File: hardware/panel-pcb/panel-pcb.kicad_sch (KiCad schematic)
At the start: 143 parts, among them J1 USB_C_Receptacle_USB2.0_16P, J10 RS-485 OUT, J11 12V_OUT, J2 SWD, J3 FSR North, J4 FSR East, J5 12V_IN, J6 FSR South, J7 FSR West, J8 RS-485 IN, J9 INT OUT, SW1 PANEL_ID, SW2 BOOTSEL, SW3 RS-485 Termination, U1 RP2040, U2 THVD1429, U3 W25Q32JV, U4 SN74AHCT125, U5 AMS1117-5.0, U6 AP7361C-33ER-13, U7 USBLC6-2SC6, U8 LM66200, X1 12MHz ABM8-272-T3

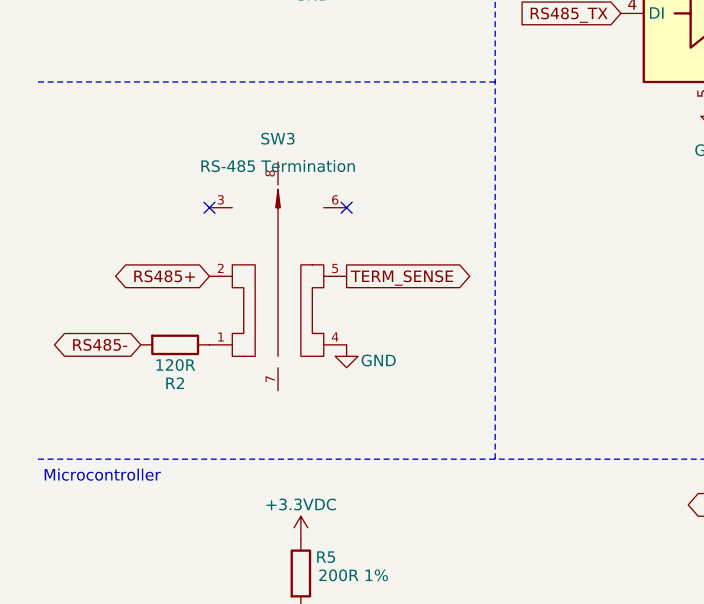
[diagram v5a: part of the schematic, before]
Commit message: Both boards: J9/J4 to the vendor WJ500V land pattern; WS2815 cap question closed
Terminal blocks now use the footprint published by the manufacturer of the part
we actually buy (KANGNEX WJ500V-5.08-2P, LCSC C8465), pulled via easyeda2kicad,
replacing the hand-built Adam Tech MRR52 pattern:
- new panel-pcb/master-pcb:TerminalBlock_WJ500V-5.08-2P (hole 1.30mm per the
  vendor recommendation vs our 1.50mm, pad 2.00mm, origin centred between pins)
  plus the vendor 3D model, which supersedes the Phoenix MKDS stand-in
- panel J9 and master J4 reassigned, re-placed and re-routed
- part metadata follows: MPN WJ500V-5.08-2P, LCSC C8465, datasheet to the LCSC
  page, stale DigiKey fields dropped

Pitch (5.08mm) and body envelope (10.16 x 10.16mm) came out of the vendor data
matching our drawing-derived numbers, so that part of the physical-verification
item is closed without parts in hand; pin-1 orientation still wants an eyeball
on arrival.

Checklist: WS2815 5V bench test waived (not worth buying parts; the substantive
check was the datasheet-variant confirm, and VIH 2.7V min is a spec guarantee).
Per-LED pin-1 caps C22-C49 CLOSED as correct — the original 2018 WS2815 doc and
WS2815B-V3 both give pin 1 as "IC POWER SUPPLY, Suspended or connected with a
filter capacitor to GROUND"; our V1 doc is the outlier calling it NC. Paper does
not prove V1 silicon brings that rail out, but a 100nF is no DC load, so the cap
is inert at worst. No per-LED VDD decoupling is wanted: the channels are
constant-current, and the vendor states no extra components are needed.

DRC 0 / schematic-parity 0 / ERC 0 on both boards, zero exclusions.
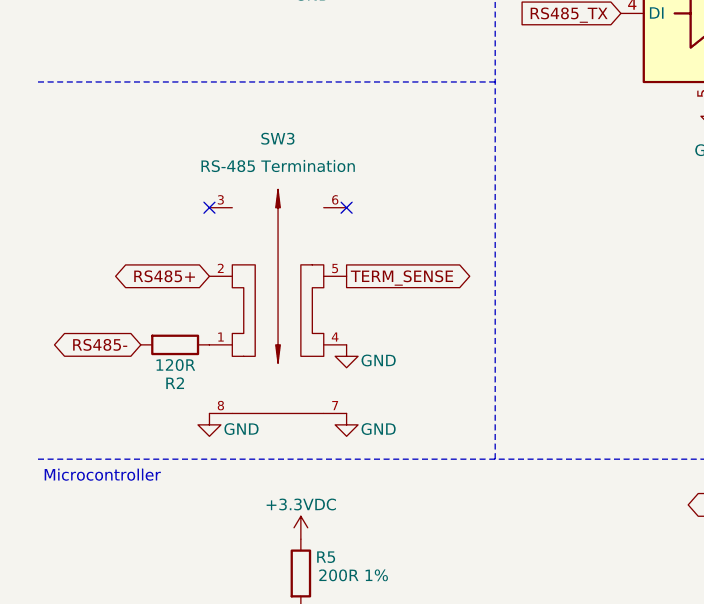
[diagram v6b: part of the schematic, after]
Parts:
- J9: footprint panel-pcb:TerminalBlock_MRR52-5.08-2P -> panel-pcb:TerminalBlock_WJ500V-5.08-2P; DigiKey 5245-MRR522-5.08-V-ND -> (none); LCSC (none) -> C8465; MPN MRR522-5.08-V -> WJ500V-5.08-2P
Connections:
- net GND: now also SW3.7, SW3.8
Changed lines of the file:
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@@
 	)
 	(symbol
+		(lib_id "power:GND")
+		(at 46.99 114.3 0)
+		(unit 1)
+		(body_style 1)
+		(exclude_from_sim no)
+		(in_bom yes)
+		(on_board yes)
+		(in_pos_files yes)
+		(dnp no)
+		(property "Reference" "#PWR0167"
+			(at 46.99 119.38 0)
+			(hide yes)
+			(show_name no)
+			(do_not_autoplace no)
+			(effects
+				(font
+					(size 1.27 1.27)
+				)
+			)
+		)
+		(property "Value" "GND"
+			(at 50.55 116.08 0)
+			(show_name no)
+			(do_not_autoplace no)
+			(effects
+				(font
+					(size 1.27 1.27)
+				)
+			)
+		)
+		(property "Footprint" ""
+			(at 46.99 114.3 0)
+			(hide yes)
+			(show_name no)
+			(do_not_autoplace no)
+			(effects
+				(font
+					(size 1.27 1.27)
+				)
+			)
+		)
+		(property "Datasheet" ""
+			(at 46.99 114.3 0)
+			(hide yes)
+			(show_name no)
+			(do_not_autoplace no)
+			(effects
+				(font
+					(size 1.27 1.27)
+				)
+			)
+		)
+		(property "Description" "Power symbol creates a global label with name \"GND\" , ground"
+			(at 46.99 114.3 0)
+			(hide yes)
+			(show_name no)
+			(do_not_autoplace no)
+			(effects
+				(font
+					(size 1.27 1.27)
+				)
+			)
+		)
+		(pin "1"
+		)
+		(instances
+			(project "panel-pcb"
+				(path "/a1b2c3d4-0000-4000-8000-000000000001"
+					(reference "#PWR0167")
+					(unit 1)
+				)
+			)
+		)
+	)
+	(symbol
 		(lib_id "power:+3V3")
 		(at 335.28 233.68 0)
@@
 			)
 		)
-		(property "Footprint" "panel-pcb:TerminalBlock_MRR52-5.08-2P"
+		(property "Footprint" "panel-pcb:TerminalBlock_WJ500V-5.08-2P"
 			(at 220.98 234.95 0)
 			(hide yes)
@@
 			)
 		)
-		(property "Datasheet" "https://dcomponents.com/uploads/375571_MRR52-5.08-V.pdf"
+		(property "Datasheet" "https://www.lcsc.com/product-detail/C8465.html"
 			(at 220.98 234.95 0)
 			(hide yes)
@@
 			)
 		)
-		(property "Description" "Adam Tech MRR522-5.08-V, 2P 5.08mm Eurostyle PCB screw terminal (INT out, single conductor used)"
+		(property "Description" "KANGNEX WJ500V-5.08-2P (LCSC C8465), 2P 5.08mm Eurostyle PCB screw terminal (INT out, single conductor used)"
 			(at 220.98 234.95 0)
 			(hide yes)
@@
 			)
 		)
-		(property "MPN" "MRR522-5.08-V"
+		(property "MPN" "WJ500V-5.08-2P"
 			(at 220.98 234.95 0)
 			(hide yes)
@@
 			)
 		)
-		(property "LCSC" ""
+		(property "LCSC" "C8465"
 			(at 220.98 234.95 0)
 			(hide yes)
@@
 			)
 		)
-		(property "DigiKey" "5245-MRR522-5.08-V-ND"
-			(at 0 0 0)
-			(hide yes)
-			(show_name no)
-			(do_not_autoplace no)
-			(effects
-				(font
-					(size 1.27 1.27)
-				)
-			)
-		)
 		(pin "1"
 		)
@@
 					(unit 1)
 				)
+			)
+		)
+	)
+	(symbol
+		(lib_id "power:GND")
+		(at 31.75 114.3 0)
+		(unit 1)
+		(body_style 1)
+		(exclude_from_sim no)
+		(in_bom yes)
+		(on_board yes)
+		(in_pos_files yes)
+		(dnp no)
+		(property "Reference" "#PWR0168"
+			(at 31.75 119.38 0)
+			(hide yes)
+			(show_name no)
+			(do_not_autoplace no)
+			(effects
+				(font
+					(size 1.27 1.27)
+				)
+			)
+		)
+		(property "Value" "GND"
+			(at 35.31 116.08 0)
+			(show_name no)
+			(do_not_autoplace no)
+			(effects
+				(font
+					(size 1.27 1.27)
+				)
+			)
+		)
+		(property "Footprint" ""
+			(at 31.75 114.3 0)
+			(hide yes)
+			(show_name no)
+			(do_not_autoplace no)
+			(effects
+				(font
+					(size 1.27 1.27)
+				)
+			)
+		)
+		(property "Datasheet" ""
+			(at 31.75 114.3 0)
+			(hide yes)
+			(show_name no)
+			(do_not_autoplace no)
+			(effects
+				(font
+					(size 1.27 1.27)
+				)
+			)
+		)
+		(property "Description" "Power symbol creates a global label with name \"GND\" , ground"
+			(at 31.75 114.3 0)
+			(hide yes)
+			(show_name no)
+			(do_not_autoplace no)
+			(effects
+				(font
+					(size 1.27 1.27)
+				)
+			)
+		)
+		(pin "1"
+		)
+		(instances
+			(project "panel-pcb"
+				(path "/a1b2c3d4-0000-4000-8000-000000000001"
+					(reference "#PWR0168")
+					(unit 1)
+				)
